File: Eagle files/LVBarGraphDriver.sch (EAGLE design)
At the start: 22 parts, among them IC1 74HC595D, IC2 74HC595D

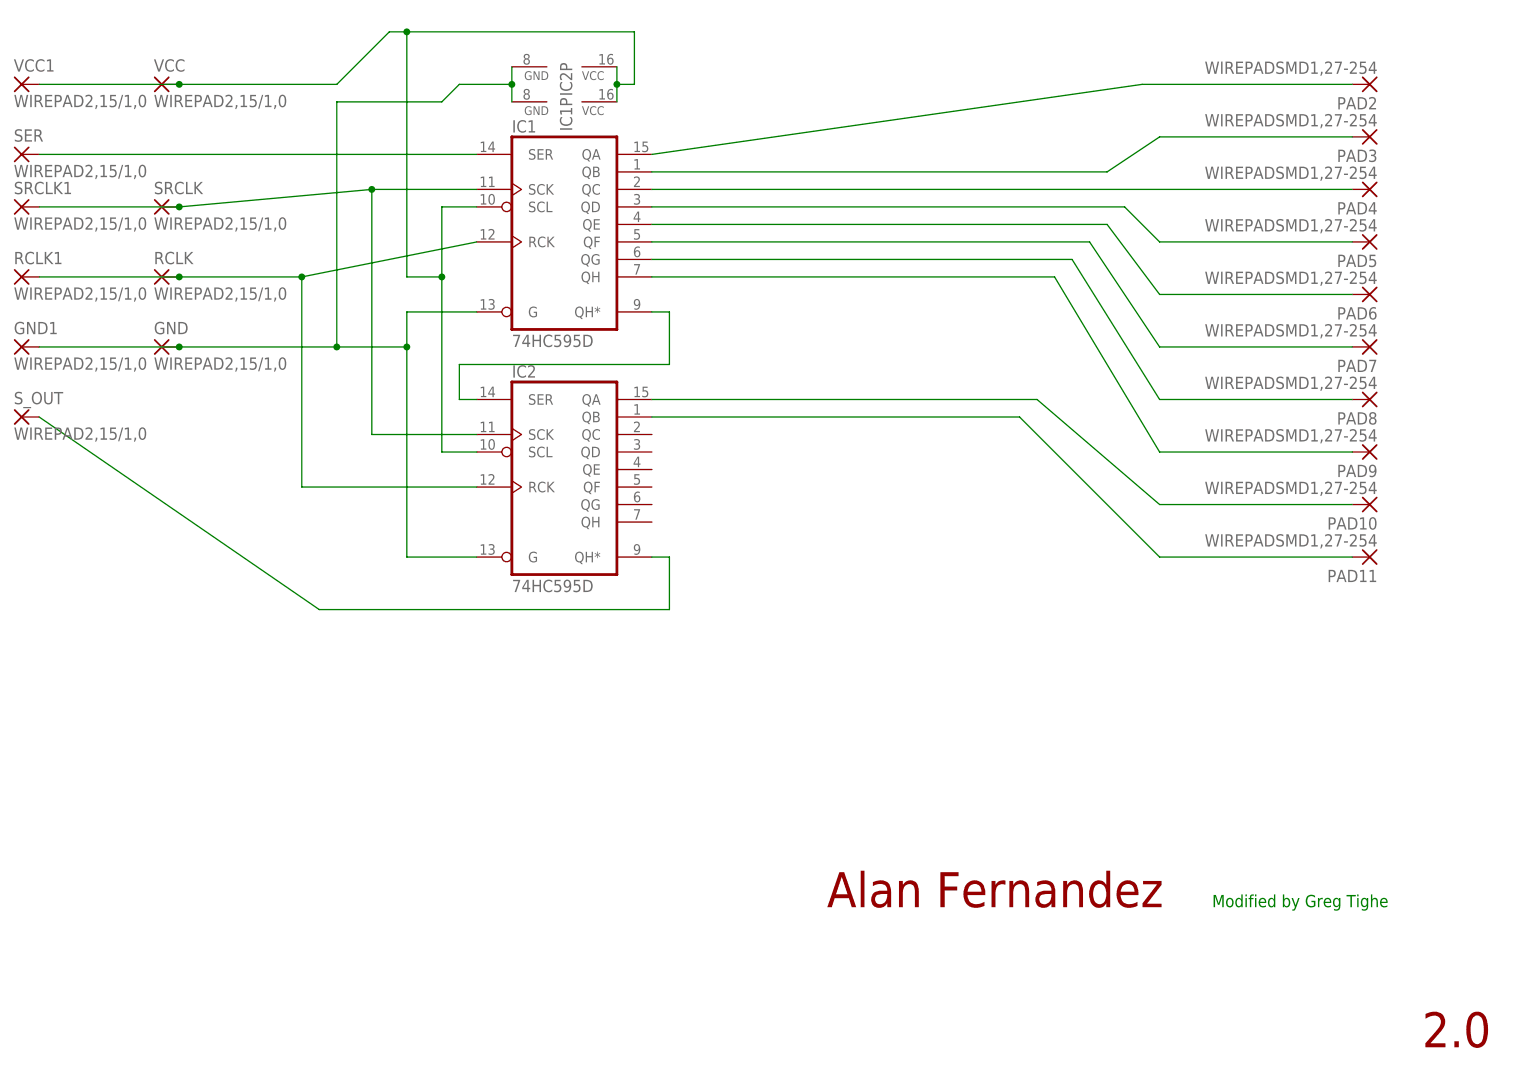
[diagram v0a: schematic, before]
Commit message: Prep for oshpark
Changed naming of BarGraphDriver to be more accurate, added a new bar
graph driver for non-lv boards, fixed the usb breakout to match our
standards and removed the text doc.
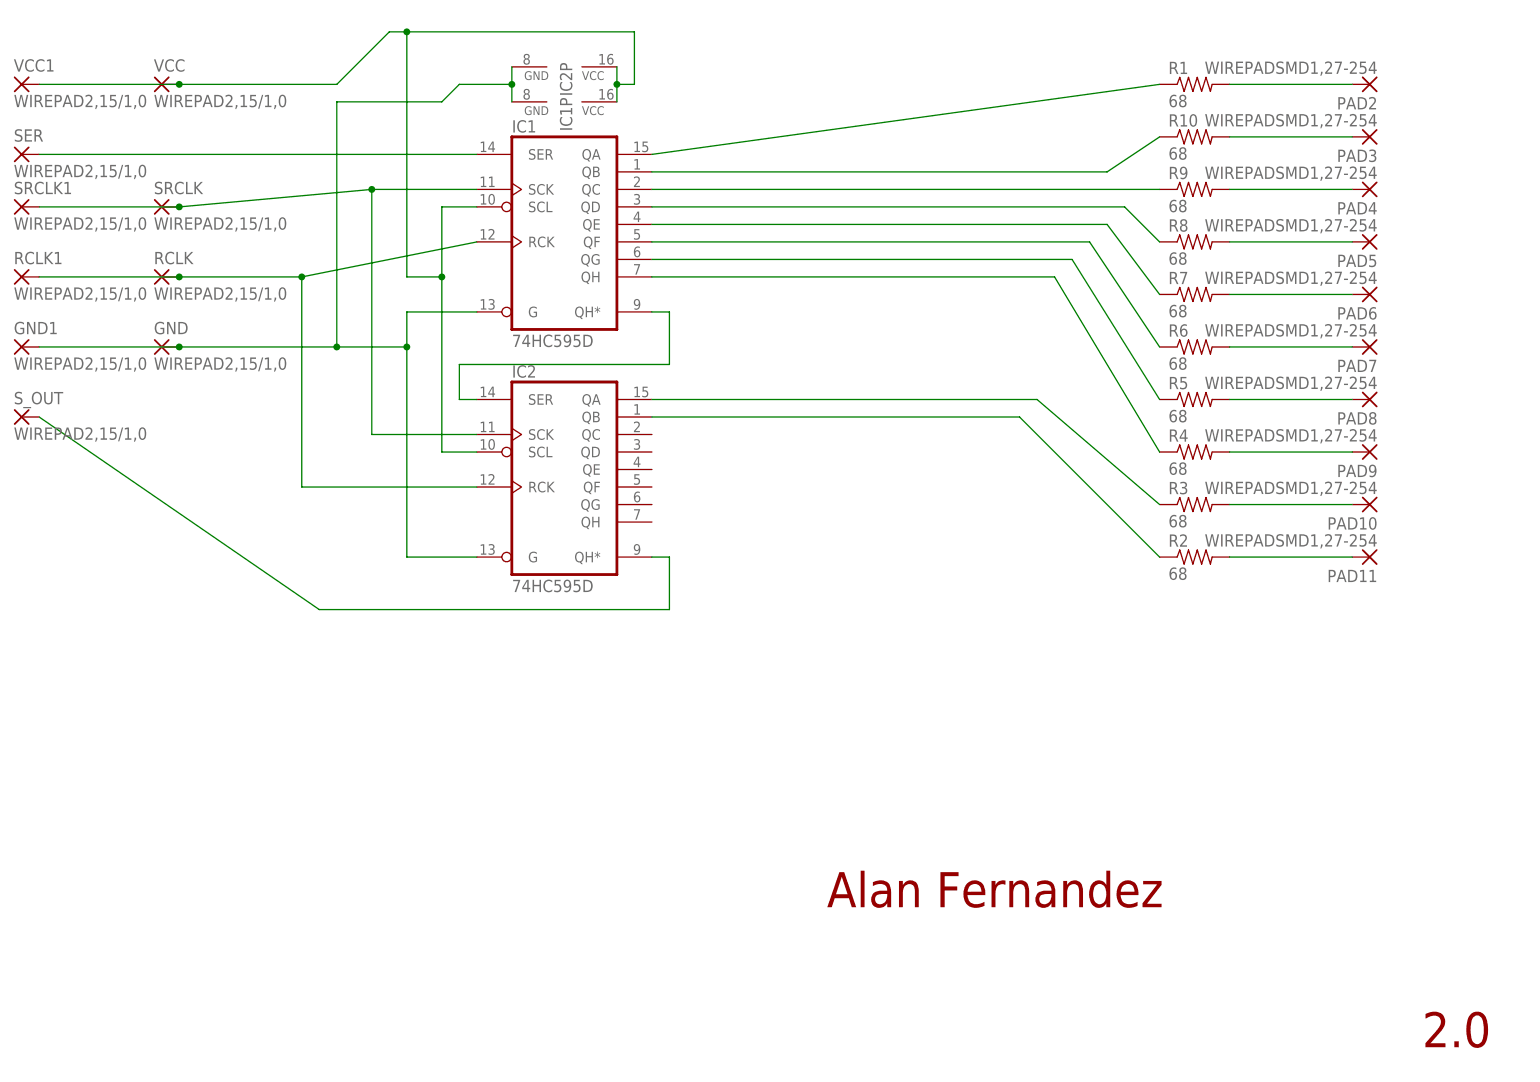
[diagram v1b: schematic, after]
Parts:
- added R1, R10, R2, R3, R4, R5, R6, R7, R8, R9: 68, SparkFun-Resistors:RESISTOR1206
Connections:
- new net N$1: PAD11.P, R2.2
- new net N$10: PAD2.P, R1.2
- new net N$2: PAD10.P, R3.2
- new net N$3: PAD9.P, R4.2
- new net N$4: PAD8.P, R5.2
- new net N$5: PAD7.P, R6.2
- new net N$6: PAD6.P, R7.2
- new net N$7: PAD5.P, R8.2
- new net N$8: PAD4.P, R9.2
- new net N$9: PAD3.P, R10.2
- net N$11: now also R1.1; no longer PAD2.P
- net N$12: now also R10.1; no longer PAD3.P
- net N$13: now also R9.1; no longer PAD4.P
- net N$14: now also R8.1; no longer PAD5.P
- net N$15: now also R7.1; no longer PAD6.P
- net N$16: now also R6.1; no longer PAD7.P
- net N$17: now also R5.1; no longer PAD8.P
- net N$18: now also R4.1; no longer PAD9.P
- net N$19: now also R3.1; no longer PAD10.P
- net N$20: now also R2.1; no longer PAD11.P
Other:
- note removed: "Modified by Greg Tighe"
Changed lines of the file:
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@@
 <part name="IC1" library="74xx-eu" deviceset="74*595" device="D" technology="HC"/>
 <part name="IC2" library="74xx-eu" deviceset="74*595" device="D" technology="HC"/>
+<part name="R1" library="SparkFun-Resistors" deviceset="RESISTOR" device="1206" value="68"/>
+<part name="R2" library="SparkFun-Resistors" deviceset="RESISTOR" device="1206" value="68"/>
+<part name="R3" library="SparkFun-Resistors" deviceset="RESISTOR" device="1206" value="68"/>
+<part name="R4" library="SparkFun-Resistors" deviceset="RESISTOR" device="1206" value="68"/>
+<part name="R5" library="SparkFun-Resistors" deviceset="RESISTOR" device="1206" value="68"/>
+<part name="R6" library="SparkFun-Resistors" deviceset="RESISTOR" device="1206" value="68"/>
+<part name="R7" library="SparkFun-Resistors" deviceset="RESISTOR" device="1206" value="68"/>
+<part name="R8" library="SparkFun-Resistors" deviceset="RESISTOR" device="1206" value="68"/>
+<part name="R9" library="SparkFun-Resistors" deviceset="RESISTOR" device="1206" value="68"/>
+<part name="R10" library="SparkFun-Resistors" deviceset="RESISTOR" device="1206" value="68"/>
 <part name="SRCLK" library="wirepad" deviceset="WIREPAD" device="2,15/1,0" value="WIREPAD2,15/1,0"/>
 <part name="RCLK" library="wirepad" deviceset="WIREPAD" device="2,15/1,0" value="WIREPAD2,15/1,0"/>
@@
 <text x="66.04" y="-48.26" size="5.08" layer="94">Alan Fernandez</text>
 <text x="152.4" y="-68.58" size="5.08" layer="94">2.0</text>
-<text x="121.92" y="-48.26" size="1.778" layer="91">Modified by Greg Tighe</text>
 </plain>
 <instances>
 <instance part="IC1" gate="A" x="27.94" y="50.8"/>
 <instance part="IC2" gate="A" x="27.94" y="15.24"/>
+<instance part="R1" gate="G$1" x="119.38" y="71.12"/>
+<instance part="R2" gate="G$1" x="119.38" y="2.54"/>
+<instance part="R3" gate="G$1" x="119.38" y="10.16"/>
+<instance part="R4" gate="G$1" x="119.38" y="17.78"/>
+<instance part="R5" gate="G$1" x="119.38" y="25.4"/>
+<instance part="R6" gate="G$1" x="119.38" y="33.02"/>
+<instance part="R7" gate="G$1" x="119.38" y="40.64"/>
+<instance part="R8" gate="G$1" x="119.38" y="48.26"/>
+<instance part="R9" gate="G$1" x="119.38" y="55.88"/>
+<instance part="R10" gate="G$1" x="119.38" y="63.5"/>
 <instance part="SRCLK" gate="G$1" x="-30.48" y="53.34"/>
 <instance part="RCLK" gate="G$1" x="-30.48" y="43.18"/>
@@
 <segment>
 <pinref part="IC1" gate="A" pin="QA"/>
-<wire x1="40.64" y1="60.96" x2="111.76" y2="71.12" width="0.1524" layer="91"/>
-<pinref part="PAD2" gate="G$1" pin="P"/>
-<wire x1="111.76" y1="71.12" x2="142.24" y2="71.12" width="0.1524" layer="91"/>
+<pinref part="R1" gate="G$1" pin="1"/>
+<wire x1="40.64" y1="60.96" x2="114.3" y2="71.12" width="0.1524" layer="91"/>
 </segment>
 </net>
@@
 <segment>
 <pinref part="IC1" gate="A" pin="QB"/>
+<pinref part="R10" gate="G$1" pin="1"/>
 <wire x1="40.64" y1="58.42" x2="106.68" y2="58.42" width="0.1524" layer="91"/>
 <wire x1="106.68" y1="58.42" x2="114.3" y2="63.5" width="0.1524" layer="91"/>
-<pinref part="PAD3" gate="G$1" pin="P"/>
-<wire x1="114.3" y1="63.5" x2="142.24" y2="63.5" width="0.1524" layer="91"/>
 </segment>
 </net>
@@
 <segment>
 <pinref part="IC1" gate="A" pin="QC"/>
-<wire x1="40.64" y1="55.88" x2="142.24" y2="55.88" width="0.1524" layer="91"/>
-<pinref part="PAD4" gate="G$1" pin="P"/>
+<wire x1="40.64" y1="55.88" x2="114.3" y2="55.88" width="0.1524" layer="91"/>
+<pinref part="R9" gate="G$1" pin="1"/>
 </segment>
 </net>
@@
 <wire x1="40.64" y1="53.34" x2="109.22" y2="53.34" width="0.1524" layer="91"/>
 <wire x1="109.22" y1="53.34" x2="114.3" y2="48.26" width="0.1524" layer="91"/>
-<pinref part="PAD5" gate="G$1" pin="P"/>
-<wire x1="114.3" y1="48.26" x2="142.24" y2="48.26" width="0.1524" layer="91"/>
+<pinref part="R8" gate="G$1" pin="1"/>
 </segment>
 </net>
@@
 <wire x1="40.64" y1="50.8" x2="106.68" y2="50.8" width="0.1524" layer="91"/>
 <wire x1="106.68" y1="50.8" x2="114.3" y2="40.64" width="0.1524" layer="91"/>
-<pinref part="PAD6" gate="G$1" pin="P"/>
-<wire x1="114.3" y1="40.64" x2="142.24" y2="40.64" width="0.1524" layer="91"/>
+<pinref part="R7" gate="G$1" pin="1"/>
 </segment>
 </net>
@@
 <wire x1="40.64" y1="48.26" x2="104.14" y2="48.26" width="0.1524" layer="91"/>
 <wire x1="104.14" y1="48.26" x2="114.3" y2="33.02" width="0.1524" layer="91"/>
-<pinref part="PAD7" gate="G$1" pin="P"/>
-<wire x1="114.3" y1="33.02" x2="142.24" y2="33.02" width="0.1524" layer="91"/>
+<pinref part="R6" gate="G$1" pin="1"/>
 </segment>
 </net>
@@
 <pinref part="IC1" gate="A" pin="QG"/>
 <wire x1="40.64" y1="45.72" x2="101.6" y2="45.72" width="0.1524" layer="91"/>
+<pinref part="R5" gate="G$1" pin="1"/>
 <wire x1="101.6" y1="45.72" x2="114.3" y2="25.4" width="0.1524" layer="91"/>
-<pinref part="PAD8" gate="G$1" pin="P"/>
-<wire x1="114.3" y1="25.4" x2="142.24" y2="25.4" width="0.1524" layer="91"/>
 </segment>
 </net>
@@
 <wire x1="40.64" y1="43.18" x2="99.06" y2="43.18" width="0.1524" layer="91"/>
 <wire x1="99.06" y1="43.18" x2="114.3" y2="17.78" width="0.1524" layer="91"/>
-<pinref part="PAD9" gate="G$1" pin="P"/>
-<wire x1="114.3" y1="17.78" x2="142.24" y2="17.78" width="0.1524" layer="91"/>
+<pinref part="R4" gate="G$1" pin="1"/>
 </segment>
 </net>
@@
 <pinref part="IC2" gate="A" pin="QA"/>
 <wire x1="40.64" y1="25.4" x2="96.52" y2="25.4" width="0.1524" layer="91"/>
+<pinref part="R3" gate="G$1" pin="1"/>
 <wire x1="96.52" y1="25.4" x2="114.3" y2="10.16" width="0.1524" layer="91"/>
-<pinref part="PAD10" gate="G$1" pin="P"/>
-<wire x1="114.3" y1="10.16" x2="142.24" y2="10.16" width="0.1524" layer="91"/>
 </segment>
 </net>
@@
 <net name="N$20" class="2">
 <segment>
+<pinref part="R2" gate="G$1" pin="1"/>
 <wire x1="114.3" y1="2.54" x2="93.98" y2="22.86" width="0.1524" layer="91"/>
 <pinref part="IC2" gate="A" pin="QB"/>
 <wire x1="93.98" y1="22.86" x2="40.64" y2="22.86" width="0.1524" layer="91"/>
+</segment>
+</net>
+<net name="N$1" class="2">
+<segment>
+<pinref part="R2" gate="G$1" pin="2"/>
 <pinref part="PAD11" gate="G$1" pin="P"/>
-<wire x1="114.3" y1="2.54" x2="142.24" y2="2.54" width="0.1524" layer="91"/>
-</segment>
-</net>
+<wire x1="142.24" y1="2.54" x2="124.46" y2="2.54" width="0.1524" layer="91"/>
+</segment>
+</net>
+<net name="N$2" class="2">
+<segment>
+<pinref part="R3" gate="G$1" pin="2"/>
+<pinref part="PAD10" gate="G$1" pin="P"/>
+<wire x1="142.24" y1="10.16" x2="124.46" y2="10.16" width="0.1524" layer="91"/>
+</segment>
+</net>
+<net name="N$3" class="2">
+<segment>
+<pinref part="R4" gate="G$1" pin="2"/>
+<pinref part="PAD9" gate="G$1" pin="P"/>
+<wire x1="142.24" y1="17.78" x2="124.46" y2="17.78" width="0.1524" layer="91"/>
+</segment>
+</net>
+<net name="N$4" class="2">
+<segment>
+<pinref part="R5" gate="G$1" pin="2"/>
+<pinref part="PAD8" gate="G$1" pin="P"/>
+<wire x1="142.24" y1="25.4" x2="124.46" y2="25.4" width="0.1524" layer="91"/>
+</segment>
+</net>
+<net name="N$5" class="2">
+<segment>
+<pinref part="R6" gate="G$1" pin="2"/>
+<pinref part="PAD7" gate="G$1" pin="P"/>
+<wire x1="142.24" y1="33.02" x2="124.46" y2="33.02" width="0.1524" layer="91"/>
+</segment>
+</net>
+<net name="N$6" class="2">
+<segment>
+<pinref part="R7" gate="G$1" pin="2"/>
+<pinref part="PAD6" gate="G$1" pin="P"/>
+<wire x1="142.24" y1="40.64" x2="124.46" y2="40.64" width="0.1524" layer="91"/>
+</segment>
+</net>
+<net name="N$7" class="2">
+<segment>
+<pinref part="R8" gate="G$1" pin="2"/>
+<pinref part="PAD5" gate="G$1" pin="P"/>
+<wire x1="142.24" y1="48.26" x2="124.46" y2="48.26" width="0.1524" layer="91"/>
+</segment>
+</net>
+<net name="N$8" class="2">
+<segment>
+<pinref part="R9" gate="G$1" pin="2"/>
+<pinref part="PAD4" gate="G$1" pin="P"/>
+<wire x1="142.24" y1="55.88" x2="124.46" y2="55.88" width="0.1524" layer="91"/>
+</segment>
+</net>
+<net name="N$9" class="2">
+<segment>
+<pinref part="R10" gate="G$1" pin="2"/>
+<pinref part="PAD3" gate="G$1" pin="P"/>
+<wire x1="142.24" y1="63.5" x2="124.46" y2="63.5" width="0.1524" layer="91"/>
+</segment>
+</net>
+<net name="N$10" class="2">
+<segment>
+<pinref part="R1" gate="G$1" pin="2"/>
+<pinref part="PAD2" gate="G$1" pin="P"/>
+<wire x1="142.24" y1="71.12" x2="124.46" y2="71.12" width="0.1524" layer="91"/>
+</segment>
+</net>

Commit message: aaaaaaaaaaaaaaaaaaaaaaaaaaaaaaaaaaaa
Cleaned up schematics, replaced wire solder points with header pin
mounts for standardization, recreated a broken file and dealt with the
confusion and insanity that followed.
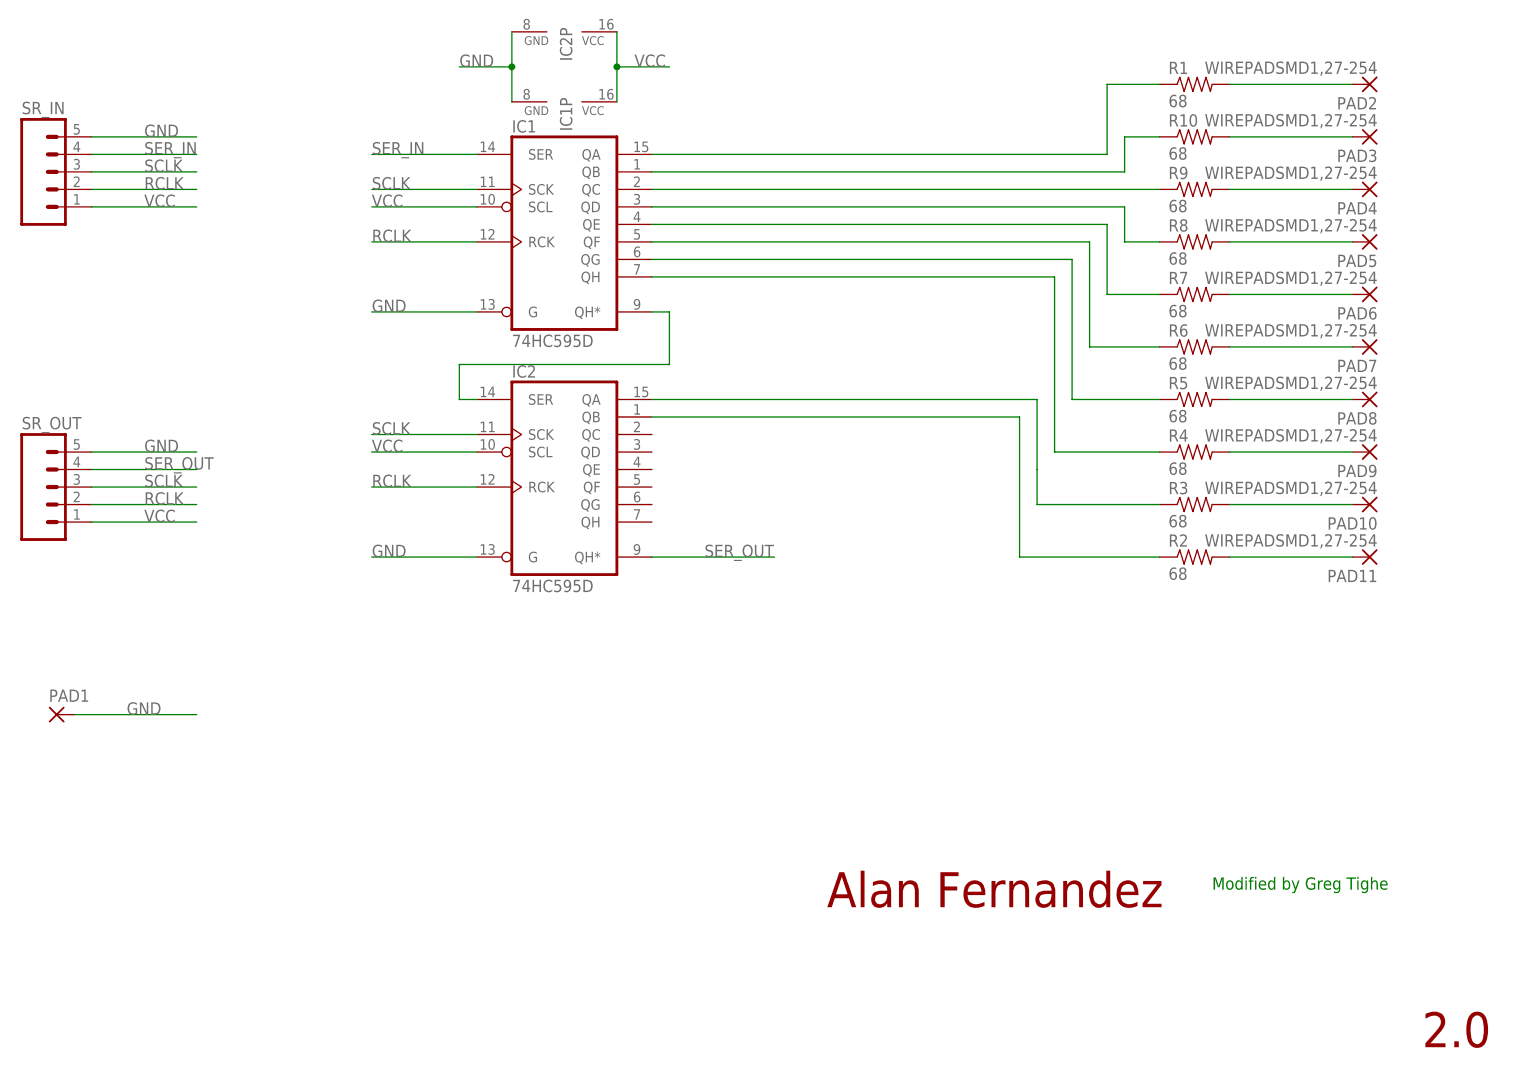
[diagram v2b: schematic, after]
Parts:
- removed GND, GND1, RCLK, RCLK1, SER, SRCLK, SRCLK1, S_OUT: WIREPAD2,15/1,0, wirepad:WIREPAD2,15/1,0
- removed VCC, VCC1: WIREPAD2,15/1,0, smallWirepadSquare:WIREPAD2,15/1,0
- added PAD1: (no value), wirepad:SMD2
- added SR_IN, SR_OUT: (no value), SparkFun-Connectors:M05PTH
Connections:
- removed net SER: IC1A.SER, SER.P
- removed net SRCLK: IC1A.SCK, IC2A.SCK, SRCLK.P, SRCLK1.P
- removed net S_OUT: IC2A.QH*, S_OUT.P
- new net SCLK: IC1A.SCK, IC2A.SCK, SR_IN.3, SR_OUT.3
- new net SER_IN: IC1A.SER, SR_IN.4
- new net SER_OUT: IC2A.QH*, SR_OUT.4
- net GND: now also PAD1.P, SR_IN.5, SR_OUT.5; no longer GND.P, GND1.P
- net RCLK: now also SR_IN.2, SR_OUT.2; no longer RCLK.P, RCLK1.P
- net VCC: now also SR_IN.1, SR_OUT.1; no longer VCC.P, VCC1.P
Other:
- note added: "Modified by Greg Tighe"
- moved on the sheet: IC2P
